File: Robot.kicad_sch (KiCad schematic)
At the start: 17 parts, among them J1 XT60 4Port PDB, J2 LM2596 Buck Converter, J3 WAGO 221 - 5 Port, J4 LM2596 Buck Converter, J5 Orange Pi 5, J6 Oak D Lite Camera, J7 LiDAR Sensor, U1 Cytron MDD10A, U2 Cytron MDD10A, U3 JGB37-520, U5 JGB37-520

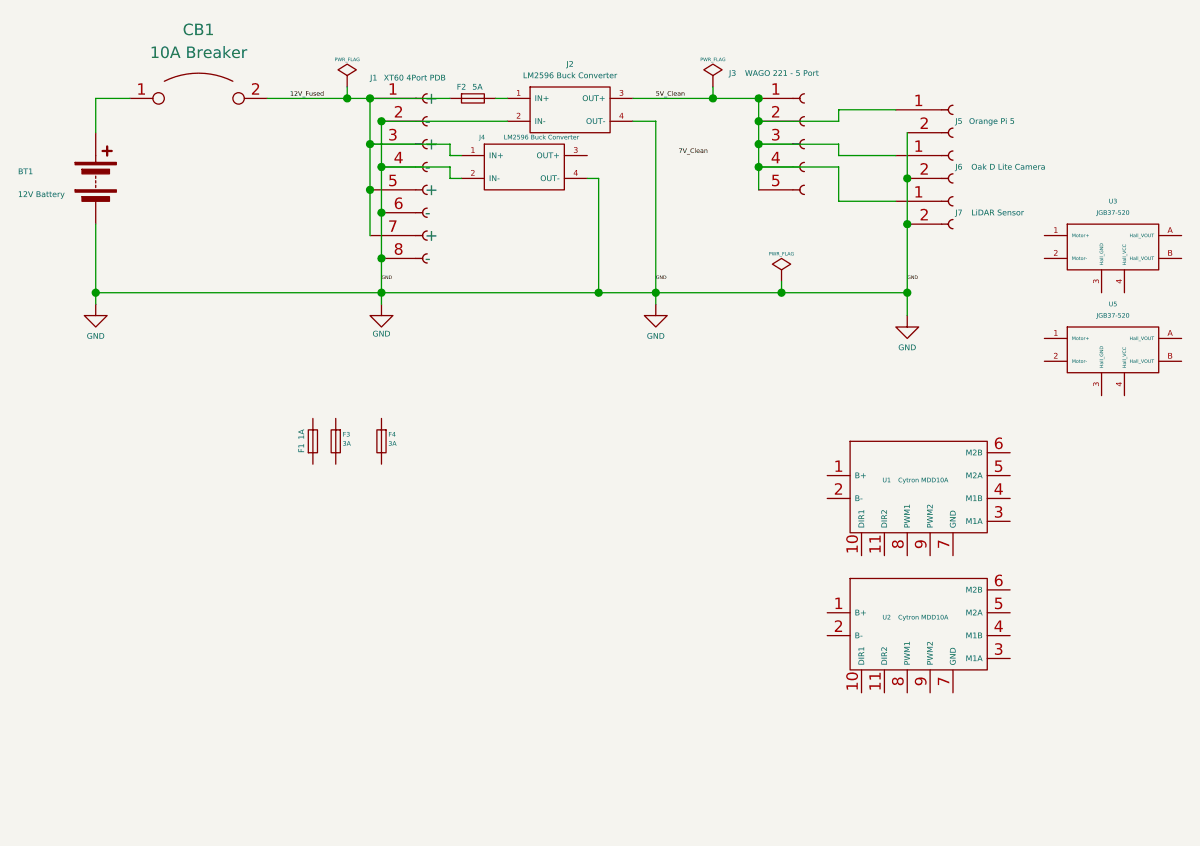
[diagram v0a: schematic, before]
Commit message: update schematic; there is now a dedicated path for the mega board, along with its own pins that we will be using for the motors
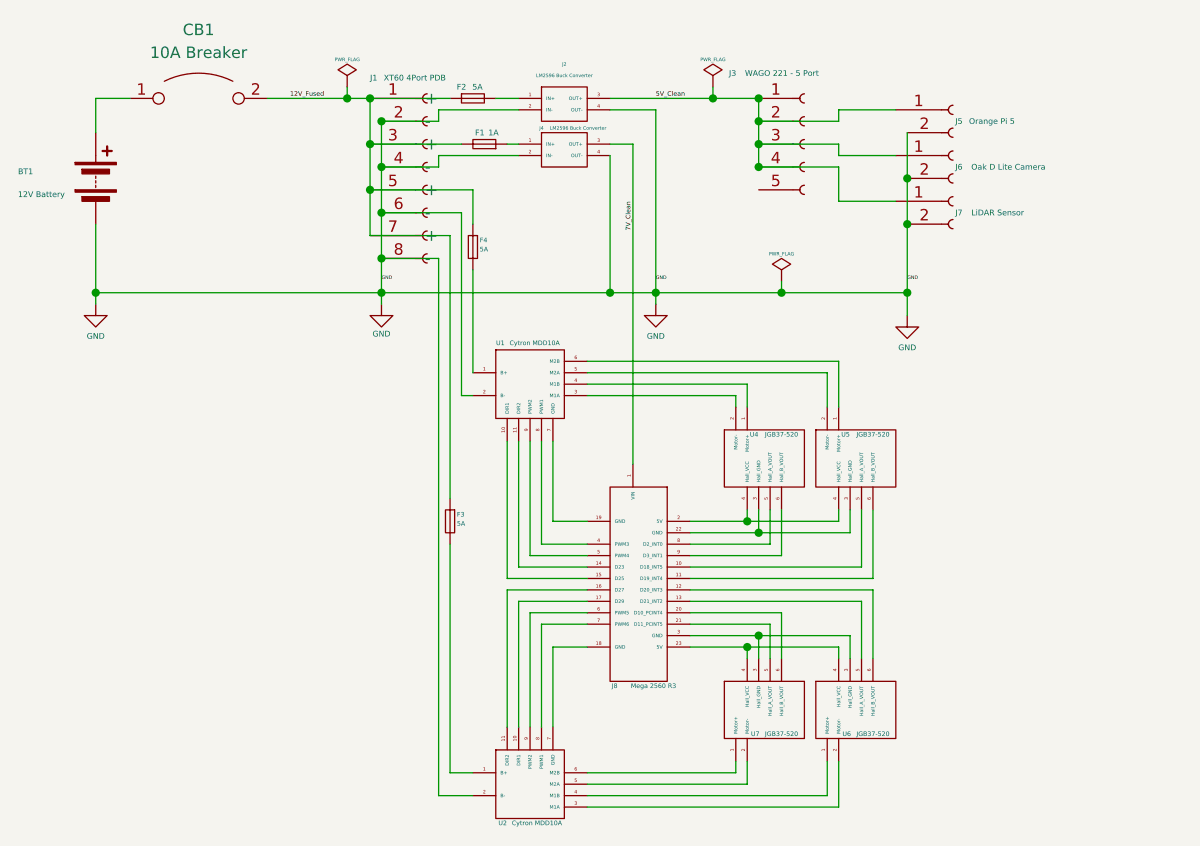
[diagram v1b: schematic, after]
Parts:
- removed U3: JGB37-520, symbol Custom_Components:JGB37-520_12V
- added J8: Mega 2560 R3, symbol Custom_Components:Elegoo_Mega_2560_R3
- added U4, U6, U7: JGB37-520, symbol Custom_Components:JGB37-520_12V
- F3, F4: value 3A -> 5A
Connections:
- net 12V_Fused: now also F1.2, F3.1, F4.1; no longer J4.1 (IN+)
- net 5V_Clean: no longer J3.5 (Pin_5)
- net 7V_Clean: now also J4.3 (OUT+), J8.1 (VIN)
- net GND: now also U1.2 (B-), U2.2 (B-)
- net at F1.1: now also J4.1 (IN+)
- net at U1.1 (B+): now also F4.2
- net at U1.10 (DIR1): now also J8.15 (D25)
- net at U1.11 (DIR2): now also J8.14 (D23)
- net at U1.3 (M1A): now also U4.2 (Motor-)
- net at U1.4 (M1B): now also U4.1 (Motor+)
- net at U1.5 (M2A): now also U5.2 (Motor-)
- net at U1.6 (M2B): now also U5.1 (Motor+)
- net at U1.7 (GND): now also J8.19 (GND)
- net at U1.8 (PWM1): now also J8.4 (PWM3)
- net at U1.9 (PWM2): now also J8.5 (PWM4)
- net at U2.1 (B+): now also F3.2
- net at U2.10 (DIR1): now also J8.17 (D29)
- net at U2.11 (DIR2): now also J8.16 (D27)
- net at U2.3 (M1A): now also U6.2 (Motor-)
- net at U2.4 (M1B): now also U6.1 (Motor+)
- net at U2.5 (M2A): now also U7.2 (Motor-)
- net at U2.6 (M2B): now also U7.1 (Motor+)
- net at U2.7 (GND): now also J8.18 (GND)
- net at U2.8 (PWM1): now also J8.7 (PWM6)
- net at U2.9 (PWM2): now also J8.6 (PWM5)
- net at U5.3 (Hall_GND): now also J8.22 (GND), U4.3 (Hall_GND)
- net at U5.4 (Hall_VCC): now also J8.2 (5V), U4.4 (Hall_VCC)
- new net: J8.3 (GND), U6.3 (Hall_GND), U7.3 (Hall_GND)
- new net: J8.23 (5V), U6.4 (Hall_VCC), U7.4 (Hall_VCC)
- new net: J8.21 (D11_PCINT5), U7.5 (Hall_A_VOUT)
- new net: J8.20 (D10_PCINT4), U7.6 (Hall_B_VOUT)
- new net: J8.10 (D18_INT5), U5.5 (Hall_A_VOUT)
- new net: J8.11 (D19_INT4), U5.6 (Hall_B_VOUT)
- new net: J8.8 (D2_INT0), U4.5 (Hall_A_VOUT)
- new net: J8.9 (D3_INT1), U4.6 (Hall_B_VOUT)
- new net: J8.12 (D20_INT3), U6.6 (Hall_B_VOUT)
- new net: J8.13 (D21_INT2), U6.5 (Hall_A_VOUT)
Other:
- moved on the sheet: F1, F3, F4
